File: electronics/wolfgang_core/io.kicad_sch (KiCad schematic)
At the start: 0 parts

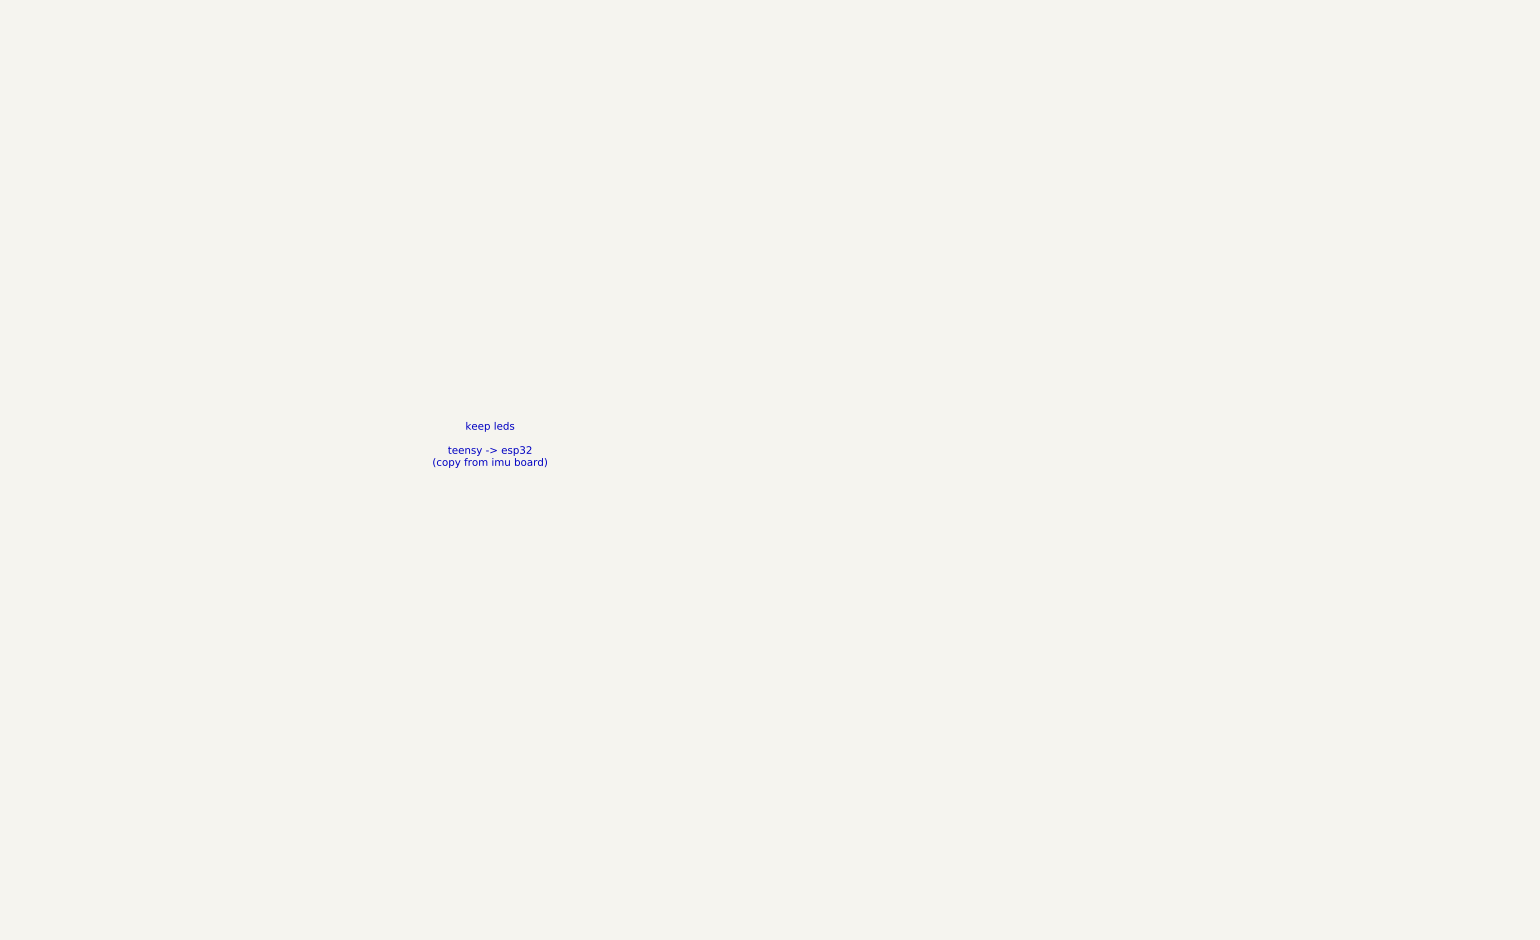
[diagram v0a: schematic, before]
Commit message: Add ESP32 in io
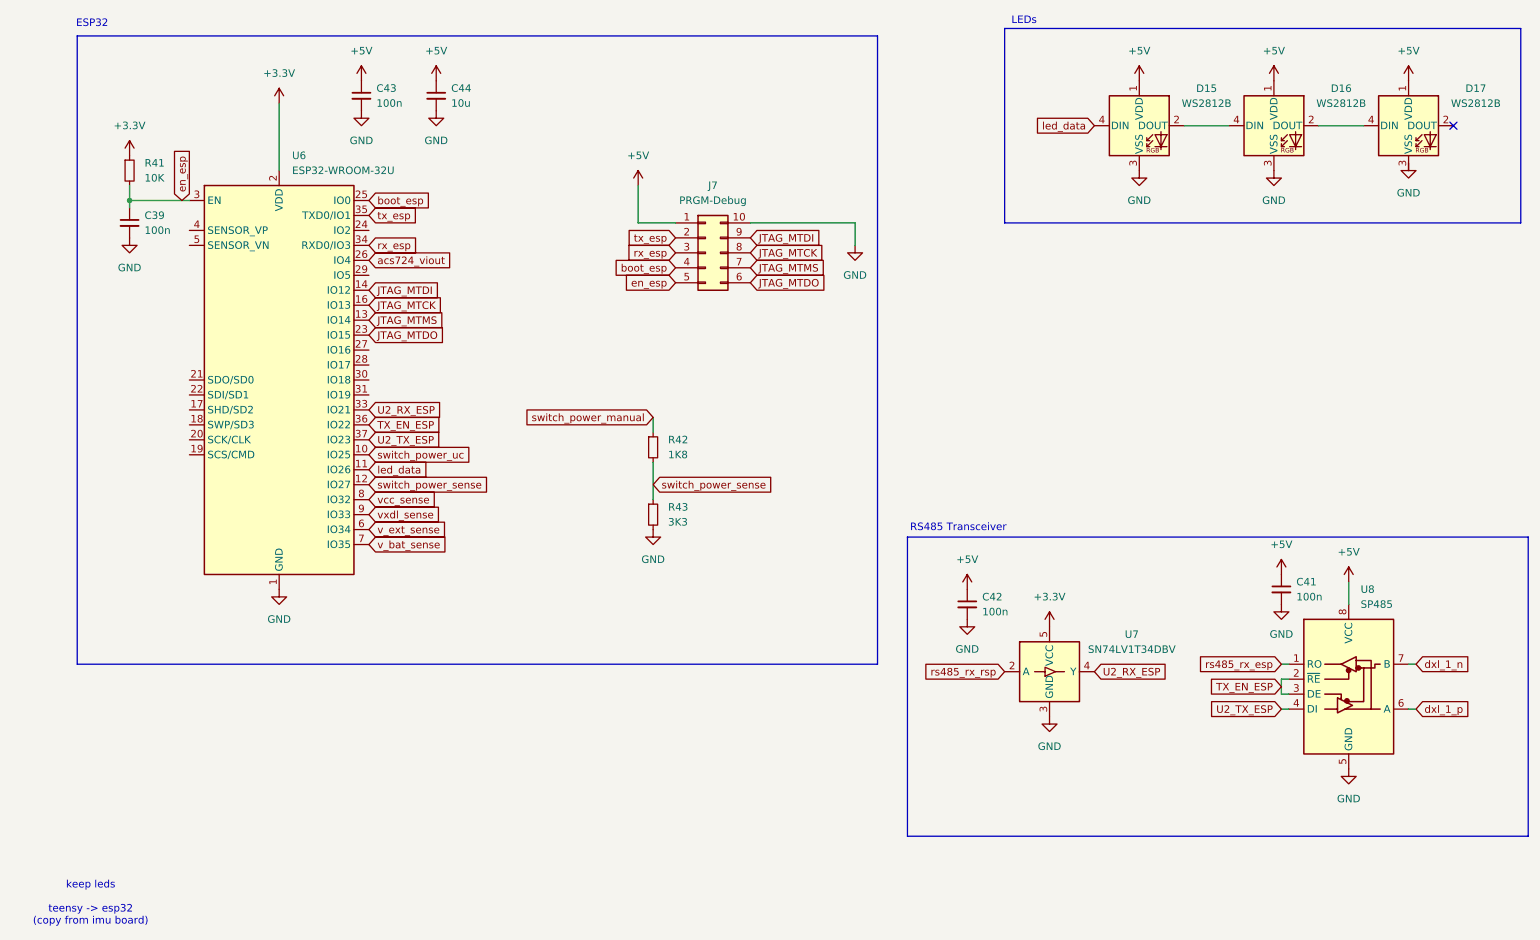
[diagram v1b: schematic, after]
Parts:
- added C39, C41, C42, C43: 100n, symbol Device:C_Small
- added C44: 10u, symbol Device:C_Small
- added D15, D16, D17: WS2812B, LED_SMD:LED_WS2812B_PLCC4_5.0x5.0mm_P3.2mm, symbol LED:WS2812B
- added J7: PRGM-Debug, symbol Connector_Generic:Conn_02x05_Counter_Clockwise
- added R41: 10K, symbol Device:R_Small
- added R42: 1K8, symbol Device:R_Small
- added R43: 3K3, symbol Device:R_Small
- added U6: ESP32-WROOM-32U, RF_Module:ESP32-WROOM-32U, symbol RF_Module:ESP32-WROOM-32U
- added U7: SN74LV1T34DBV, Package_TO_SOT_SMD:SOT-23-5, symbol Logic_LevelTranslator:SN74LV1T34DBV
- added U8: SP485, symbol Interface_UART:MAX485E
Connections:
- new net: D15.2 (DOUT), D16.4 (DIN)
- new net: D16.2 (DOUT), D17.4 (DIN)
- new net +3.3V: R41.1, U6.2 (VDD), U7.5 (VCC)
- new net +5V: C41.1, C42.1, C43.1, C44.1, D15.1 (VDD), D16.1 (VDD), D17.1 (VDD), J7.1 (Pin_1), U8.8 (VCC)
- new net GND: C39.2, C41.2, C42.2, C43.2, C44.2, D15.3 (VSS), D16.3 (VSS), J7.10 (Pin_10), R43.2, U6.1 (GND), U6.15 (GND), U6.38 (GND), U6.39 (GND), U7.3 (GND), U8.5 (GND)
- new net JTAG_MTCK: J7.8 (Pin_8), U6.16 (IO13)
- new net JTAG_MTDI: J7.9 (Pin_9), U6.14 (IO12)
- new net JTAG_MTDO: J7.6 (Pin_6), U6.23 (IO15)
- new net JTAG_MTMS: J7.7 (Pin_7), U6.13 (IO14)
- new net TX_EN_ESP: U6.36 (IO22), U8.2 (~{RE}), U8.3 (DE)
- new net U2_RX_ESP: U6.33 (IO21), U7.4 (Y)
- new net U2_TX_ESP: U6.37 (IO23), U8.4 (DI)
- new net acs724_viout: U6.26 (IO4)
- new net boot_esp: J7.4 (Pin_4), U6.25 (IO0)
- new net dxl_1_n: U8.7 (B)
- new net dxl_1_p: U8.6 (A)
- new net en_esp: C39.1, J7.5 (Pin_5), R41.2, U6.3 (EN)
- new net led_data: D15.4 (DIN), U6.11 (IO26)
- new net rs485_rx_esp: U8.1 (RO)
- new net rs485_rx_rsp: U7.2 (A)
- new net rx_esp: J7.3 (Pin_3), U6.34 (RXD0/IO3)
- new net switch_power_manual: R42.1
- new net switch_power_sense: R42.2, R43.1, U6.12 (IO27)
- new net switch_power_uc: U6.10 (IO25)
- new net tx_esp: J7.2 (Pin_2), U6.35 (TXD0/IO1)
- new net v_bat_sense: U6.7 (IO35)
- new net v_ext_sense: U6.6 (IO34)
- new net vcc_sense: U6.8 (IO32)
- new net vxdl_sense: U6.9 (IO33)
- no-connect marks 0 -> 1
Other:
- note added: "ESP32"
- note added: "LEDs"
- note added: "RS485 Transceiver"

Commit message: Rearrange pins
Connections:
- net switch_power_sense: now also U6.4 (SENSOR_VP); no longer U6.12 (IO27)
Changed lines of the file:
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@@
+	(wire
+		(pts
+			(xy 48.26 54.61) (xy 46.99 54.61)
+		)
+		(stroke
+			(width 0)
+			(type default)
+		)
+	)
 	(wire
 		(pts
@@
 	(wire
 		(pts
+			(xy 46.99 67.31) (xy 44.45 67.31)
+		)
+		(stroke
+			(width 0)
+			(type default)
+		)
+	)
+	(wire
+		(pts
 			(xy 124.46 46.99) (xy 124.46 53.34)
 		)
@@
 		(pts
 			(xy 233.68 130.81) (xy 233.68 133.35)
+		)
+		(stroke
+			(width 0)
+			(type default)
+		)
+	)
+	(wire
+		(pts
+			(xy 46.99 54.61) (xy 46.99 67.31)
 		)
 		(stroke
@@
 	)
 	(rectangle
-		(start 29.21 21.59)
+		(start 21.59 21.59)
 		(end 165.1 128.27)
 		(stroke
@@
 	(global_label "switch_power_sense"
 		(shape input)
-		(at 78.74 97.79 0)
-		(fields_autoplaced yes)
-		(effects
-			(font
-				(size 1.27 1.27)
-			)
-			(justify left)
-		)
-		(property "Intersheetrefs" "${INTERSHEET_REFS}"
-			(at 100.4728 97.79 0)
-			(effects
-				(font
-					(size 1.27 1.27)
-				)
-				(justify left)
-				(hide yes)
-			)
+		(at 44.45 67.31 180)
+		(fields_autoplaced yes)
+		(effects
+			(font
+				(size 1.27 1.27)
+			)
+			(justify right)
+		)
+		(property "Intersheetrefs" "${INTERSHEET_REFS}"
+			(at 22.7172 67.31 0)
+			(effects
+				(font
+					(size 1.27 1.27)
+				)
+				(justify right)
+				(hide yes)
+			)

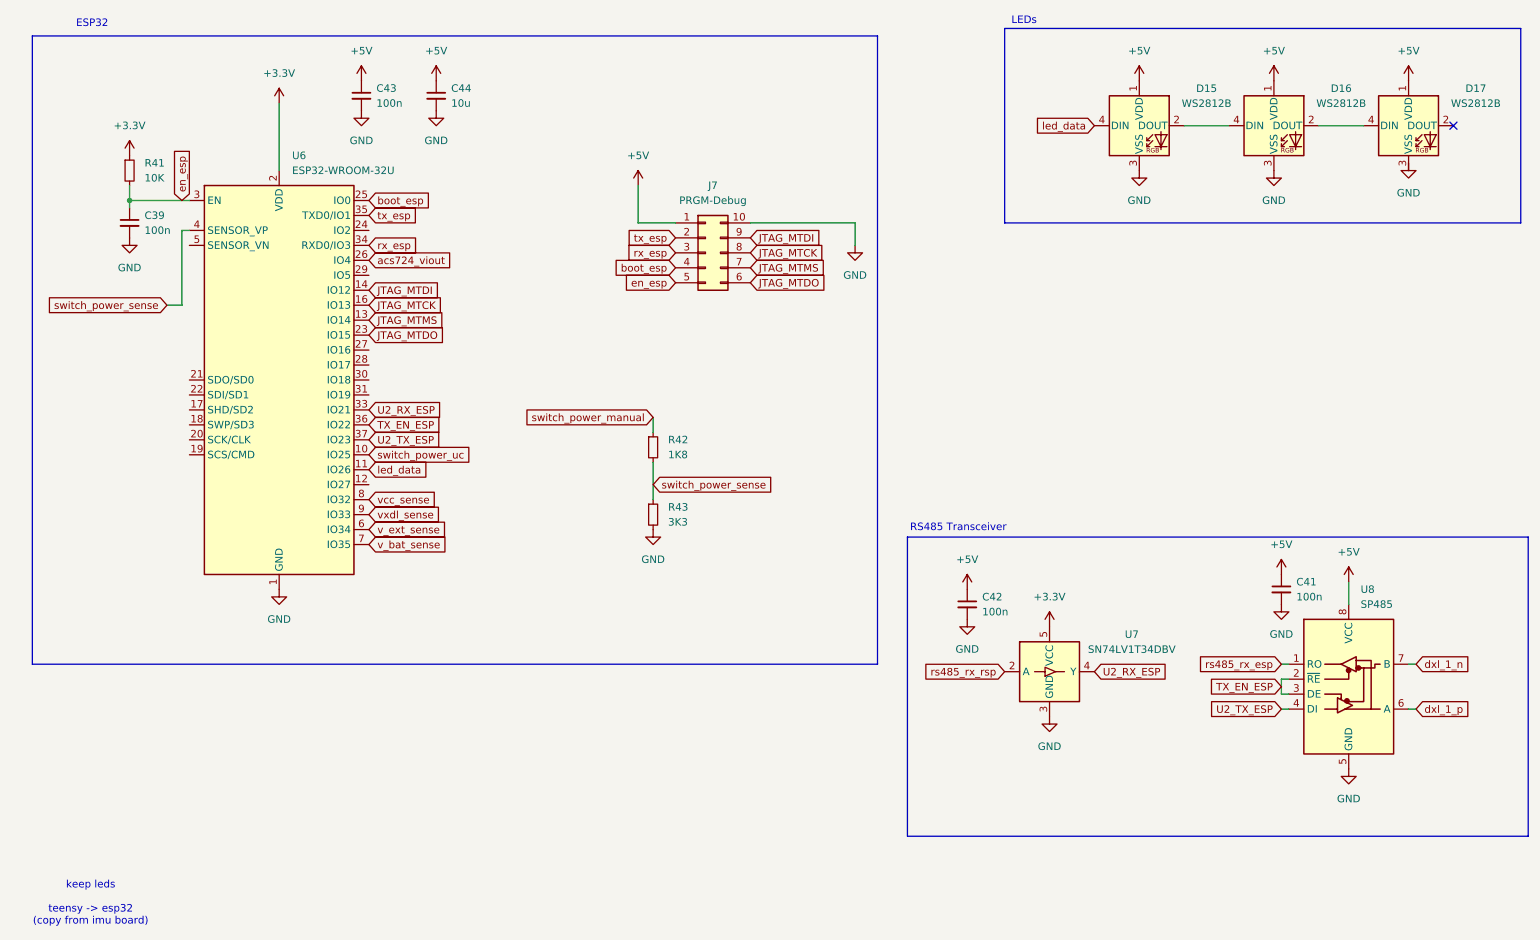
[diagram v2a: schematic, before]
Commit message: Footprints hinzugefügt
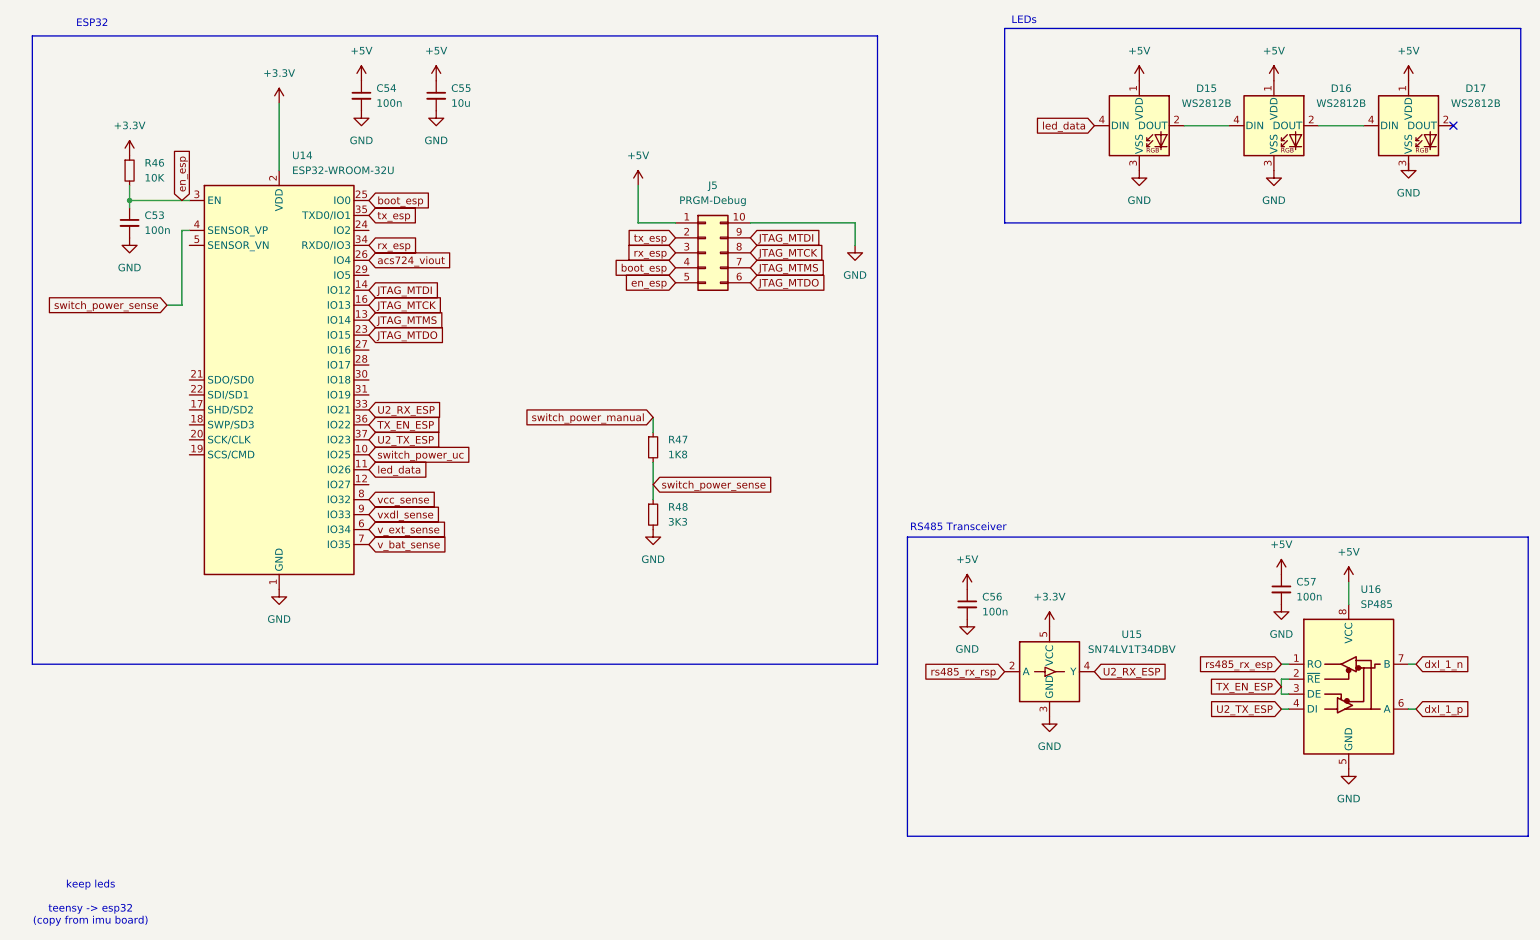
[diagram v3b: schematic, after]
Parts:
- U16: renamed from U8; footprint (none) -> Package_SO:SOIC-8_3.9x4.9mm_P1.27mm
- renumbered C39 to C53, C43 to C54, C44 to C55, C42 to C56, C41 to C57, J7 to J5, R41 to R46, R42 to R47, R43 to R48, U6 to U14, U7 to U15

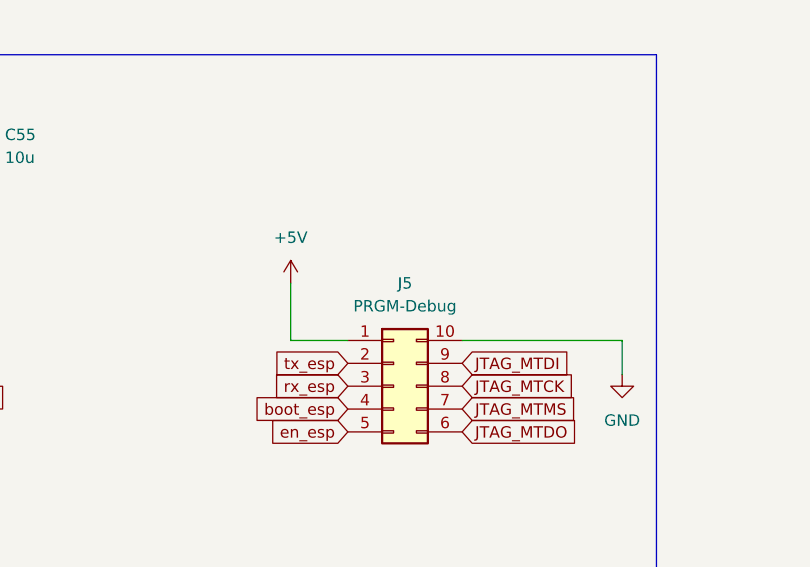
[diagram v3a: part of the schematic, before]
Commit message: Assign almost all Footprints
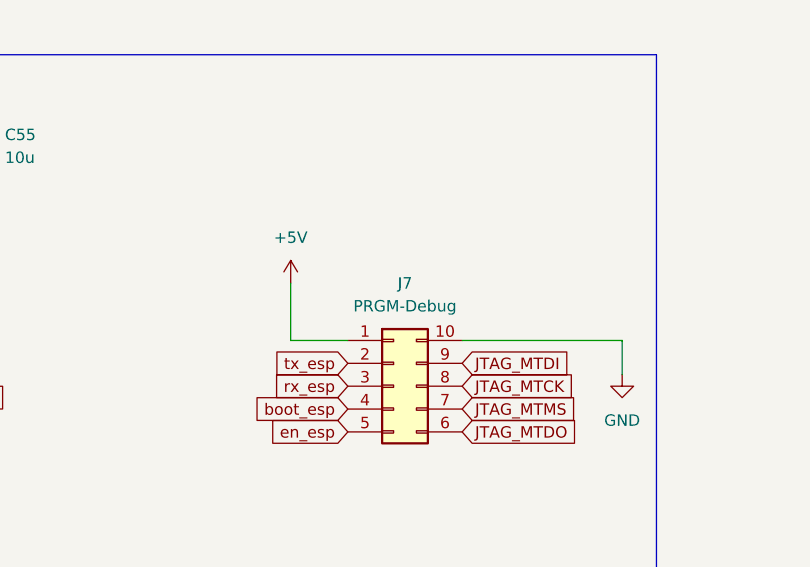
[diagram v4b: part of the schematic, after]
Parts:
- C53, C54, C55, C56, C57: footprint (none) -> Capacitor_SMD:C_0805_2012Metric
- J7: renamed from J5; footprint (none) -> bitbots:esp32_prgm_debug
- R46, R47, R48: footprint (none) -> Resistor_SMD:R_0805_2012Metric
